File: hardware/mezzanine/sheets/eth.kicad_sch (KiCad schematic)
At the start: 6 parts, among them U3 TPD4EUSB30, U4 TPD4EUSB30, U5 MagJack-A70-112-331N126

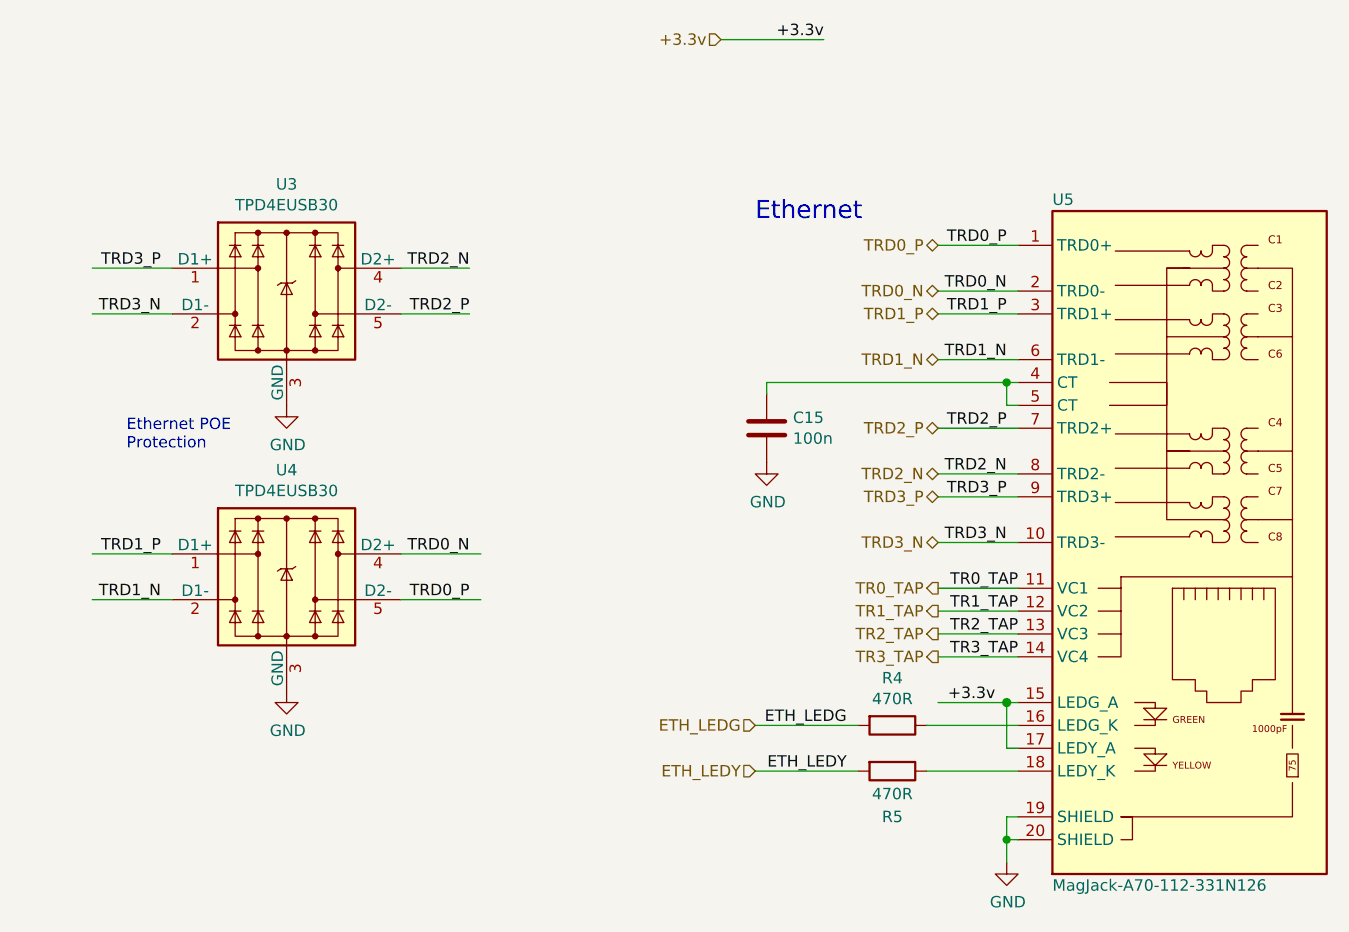
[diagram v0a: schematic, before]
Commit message: finished mezzanine signal routing
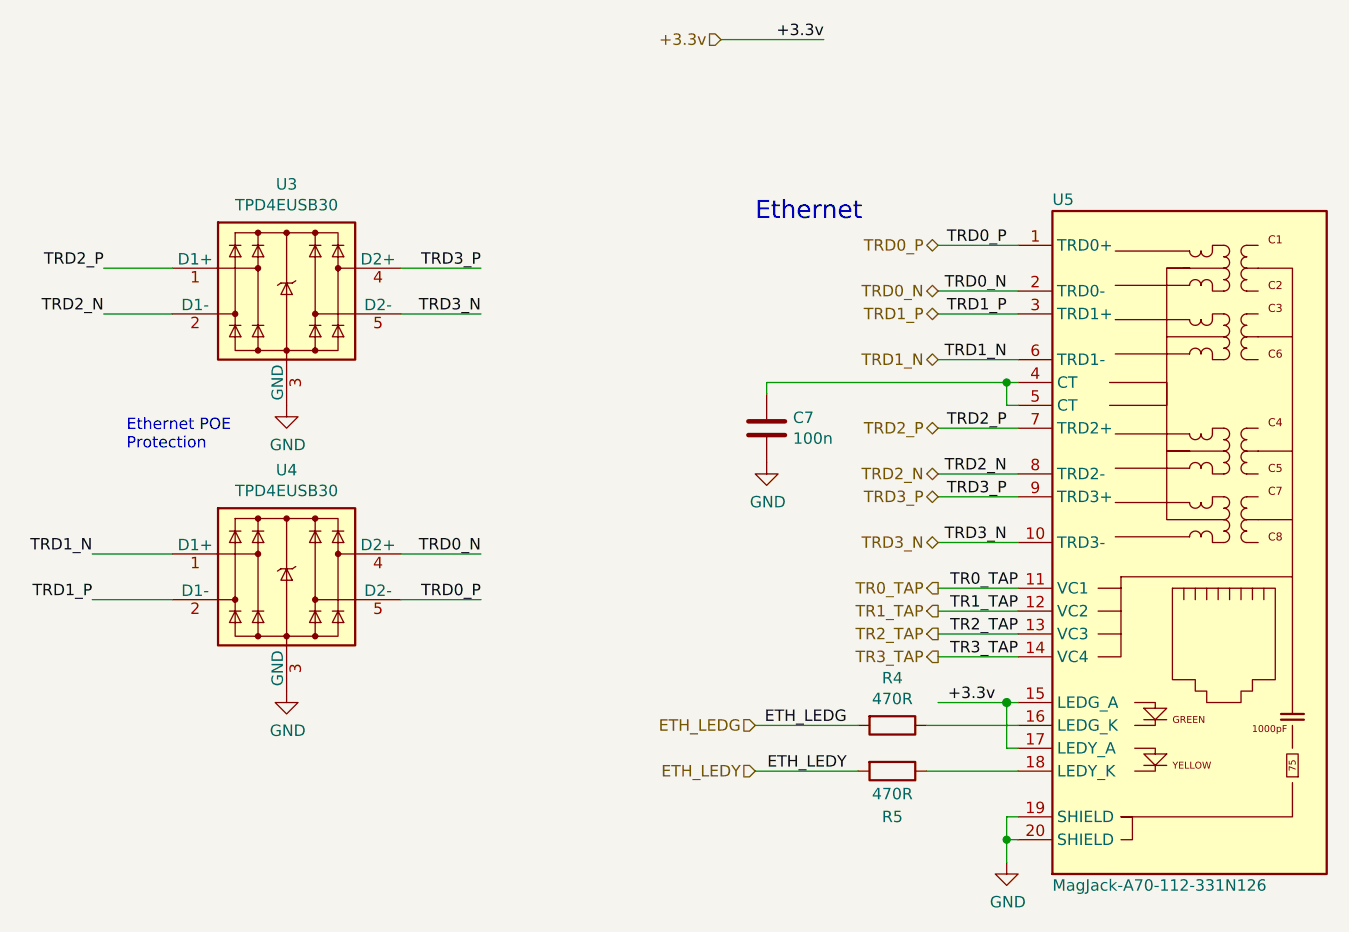
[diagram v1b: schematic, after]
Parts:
- C7: renamed from C15; footprint Capacitor_SMD:C_0402_1005Metric -> Capacitor_SMD:C_0603_1608Metric; Field4 Farnell -> (none); Field5 2611911 -> (none); Field6 RM EMK105 B7104KV-F -> (none); Field7 TAIYO YUDEN EUROPE GMBH -> (none); Field8 110091611 -> (none); Part Description 0.1uF 10% 16V Ceramic Capacitor X7R 0402 (1005 Metric) -> (none)
- R4, R5: footprint Resistor_SMD:R_0402_1005Metric -> Resistor_SMD:R_0603_1608Metric; Field4 Farnell -> (none); Field5 9239197 -> (none); Field6 RK73G1ETQTP4700D -> (none); Field7 KOA EUROPE GMBH -> (none); Field8 120887981 -> (none); Part Description Resistor 470R M1005 1% 63mW -> (none)
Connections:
- net TRD1_N: now also U4.1 (D1+), U4.10; no longer U4.2 (D1-), U4.9
- net TRD1_P: now also U4.2 (D1-), U4.9; no longer U4.1 (D1+), U4.10
- net TRD2_N: now also U3.2 (D1-), U3.9; no longer U3.4 (D2+), U3.7
- net TRD2_P: now also U3.1 (D1+), U3.10; no longer U3.5 (D2-), U3.6
- net TRD3_N: now also U3.5 (D2-), U3.6; no longer U3.2 (D1-), U3.9
- net TRD3_P: now also U3.4 (D2+), U3.7; no longer U3.1 (D1+), U3.10
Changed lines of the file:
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@@
   (junction (at 154.94 104.14) (diameter 1.016) (color 0 0 0 0))
   (junction (at 154.94 119.38) (diameter 0.9144) (color 0 0 0 0))
-  (wire (pts (xy 53.34 55.88) (xy 62.23 55.88))
-    (stroke (width 0) (type solid) (color 0 0 0 0))
-  )
-  (wire (pts (xy 53.34 60.96) (xy 62.23 60.96))
-    (stroke (width 0) (type solid) (color 0 0 0 0))
-  )
-  (wire (pts (xy 53.34 87.63) (xy 62.23 87.63))
-    (stroke (width 0) (type solid) (color 0 0 0 0))
-  )
-  (wire (pts (xy 62.23 92.71) (xy 53.34 92.71))
-    (stroke (width 0) (type solid) (color 0 0 0 0))
-  )
-  (wire (pts (xy 87.63 55.88) (xy 95.25 55.88))
-    (stroke (width 0) (type solid) (color 0 0 0 0))
-  )
-  (wire (pts (xy 87.63 60.96) (xy 95.25 60.96))
+  (wire (pts (xy 53.34 92.71) (xy 62.23 92.71))
+    (stroke (width 0) (type solid) (color 0 0 0 0))
+  )
+  (wire (pts (xy 54.61 55.88) (xy 62.23 55.88))
+    (stroke (width 0) (type solid) (color 0 0 0 0))
+  )
+  (wire (pts (xy 54.61 60.96) (xy 62.23 60.96))
+    (stroke (width 0) (type solid) (color 0 0 0 0))
+  )
+  (wire (pts (xy 62.23 87.63) (xy 53.34 87.63))
+    (stroke (width 0) (type solid) (color 0 0 0 0))
+  )
+  (wire (pts (xy 87.63 55.88) (xy 96.52 55.88))
+    (stroke (width 0) (type solid) (color 0 0 0 0))
+  )
+  (wire (pts (xy 87.63 60.96) (xy 96.52 60.96))
     (stroke (width 0) (type solid) (color 0 0 0 0))
   )
@@
     (effects (font (size 2.0066 2.0066)) (justify left bottom))
   )
-  (label "TRD3_P" (at 60.96 55.88 180)
-    (effects (font (size 1.27 1.27)) (justify right bottom))
-  )
-  (label "TRD3_N" (at 60.96 60.96 180)
-    (effects (font (size 1.27 1.27)) (justify right bottom))
-  )
-  (label "TRD1_P" (at 60.96 87.63 180)
-    (effects (font (size 1.27 1.27)) (justify right bottom))
-  )
-  (label "TRD1_N" (at 60.96 92.71 180)
-    (effects (font (size 1.27 1.27)) (justify right bottom))
-  )
-  (label "TRD2_N" (at 95.25 55.88 180)
-    (effects (font (size 1.27 1.27)) (justify right bottom))
-  )
-  (label "TRD2_P" (at 95.25 60.96 180)
-    (effects (font (size 1.27 1.27)) (justify right bottom))
-  )
-  (label "TRD0_N" (at 95.25 87.63 180)
-    (effects (font (size 1.27 1.27)) (justify right bottom))
-  )
-  (label "TRD0_P" (at 95.25 92.71 180)
+  (label "TRD1_N" (at 53.34 87.63 180)
+    (effects (font (size 1.27 1.27)) (justify right bottom))
+  )
+  (label "TRD1_P" (at 53.34 92.71 180)
+    (effects (font (size 1.27 1.27)) (justify right bottom))
+  )
+  (label "TRD2_P" (at 54.61 55.88 180)
+    (effects (font (size 1.27 1.27)) (justify right bottom))
+  )
+  (label "TRD2_N" (at 54.61 60.96 180)
+    (effects (font (size 1.27 1.27)) (justify right bottom))
+  )
+  (label "TRD3_P" (at 96.52 55.88 180)
+    (effects (font (size 1.27 1.27)) (justify right bottom))
+  )
+  (label "TRD3_N" (at 96.52 60.96 180)
+    (effects (font (size 1.27 1.27)) (justify right bottom))
+  )
+  (label "TRD0_N" (at 96.52 87.63 180)
+    (effects (font (size 1.27 1.27)) (justify right bottom))
+  )
+  (label "TRD0_P" (at 96.52 92.71 180)
     (effects (font (size 1.27 1.27)) (justify right bottom))
   )
@@
   (symbol (lib_id "power:GND") (at 74.93 71.12 0) (unit 1)
     (in_bom yes) (on_board yes)
-    (property "Reference" "#PWR068" (id 0) (at 74.93 77.47 0)
+    (property "Reference" "#PWR046" (id 0) (at 74.93 77.47 0)
       (effects (font (size 1.27 1.27)) hide)
     )
@@
   (symbol (lib_id "power:GND") (at 74.93 102.87 0) (unit 1)
     (in_bom yes) (on_board yes)
-    (property "Reference" "#PWR070" (id 0) (at 74.93 109.22 0)
+    (property "Reference" "#PWR048" (id 0) (at 74.93 109.22 0)
       (effects (font (size 1.27 1.27)) hide)
     )
@@
   (symbol (lib_id "power:GND") (at 128.27 77.47 0) (unit 1)
     (in_bom yes) (on_board yes)
-    (property "Reference" "#PWR069" (id 0) (at 128.27 83.82 0)
+    (property "Reference" "#PWR047" (id 0) (at 128.27 83.82 0)
       (effects (font (size 1.27 1.27)) hide)
     )
@@
   (symbol (lib_id "power:GND") (at 154.94 121.92 0) (unit 1)
     (in_bom yes) (on_board yes)
-    (property "Reference" "#PWR071" (id 0) (at 154.94 128.27 0)
+    (property "Reference" "#PWR049" (id 0) (at 154.94 128.27 0)
       (effects (font (size 1.27 1.27)) hide)
     )
@@
     (property "Reference" "R4" (id 0) (at 142.24 101.4222 90))
     (property "Value" "470R" (id 1) (at 142.24 103.7336 90))
-    (property "Footprint" "Resistor_SMD:R_0402_1005Metric" (id 2) (at 142.24 104.902 90)
-      (effects (font (size 1.27 1.27)) hide)
-    )
-    (property "Datasheet" "https://fscdn.rohm.com/en/products/databook/datasheet/passive/resistor/chip_resistor/mcr-e.pdf" (id 3) (at 142.24 106.68 0)
-      (effects (font (size 1.27 1.27)) hide)
-    )
-    (property "Field4" "Farnell" (id 4) (at 142.24 106.68 0)
-      (effects (font (size 1.27 1.27)) hide)
-    )
-    (property "Field5" "9239197" (id 5) (at 142.24 106.68 0)
-      (effects (font (size 1.27 1.27)) hide)
-    )
-    (property "Field7" "KOA EUROPE GMBH" (id 6) (at 142.24 106.68 0)
-      (effects (font (size 1.27 1.27)) hide)
-    )
-    (property "Field6" "RK73G1ETQTP4700D         " (id 7) (at 142.24 106.68 0)
-      (effects (font (size 1.27 1.27)) hide)
-    )
-    (property "Field8" "120887981" (id 8) (at 142.24 106.68 0)
-      (effects (font (size 1.27 1.27)) hide)
-    )
-    (property "Part Description" "Resistor 470R M1005 1% 63mW" (id 9) (at 142.24 106.68 0)
+    (property "Footprint" "Resistor_SMD:R_0603_1608Metric" (id 2) (at 142.24 104.902 90)
+      (effects (font (size 1.27 1.27)) hide)
+    )
+    (property "Datasheet" "~" (id 3) (at 142.24 106.68 0)
       (effects (font (size 1.27 1.27)) hide)
     )
@@
     (property "Reference" "R5" (id 0) (at 142.24 116.84 90))
     (property "Value" "470R" (id 1) (at 142.24 114.3 90))
-    (property "Footprint" "Resistor_SMD:R_0402_1005Metric" (id 2) (at 142.24 109.982 90)
-      (effects (font (size 1.27 1.27)) hide)
-    )
-    (property "Datasheet" "https://fscdn.rohm.com/en/products/databook/datasheet/passive/resistor/chip_resistor/mcr-e.pdf" (id 3) (at 142.24 111.76 0)
-      (effects (font (size 1.27 1.27)) hide)
-    )
-    (property "Field4" "Farnell" (id 4) (at 142.24 111.76 0)
-      (effects (font (size 1.27 1.27)) hide)
-    )
-    (property "Field5" "9239197" (id 5) (at 142.24 111.76 0)
-      (effects (font (size 1.27 1.27)) hide)
-    )
-    (property "Field7" "KOA EUROPE GMBH" (id 6) (at 142.24 111.76 0)
-      (effects (font (size 1.27 1.27)) hide)
-    )
-    (property "Field6" "RK73G1ETQTP4700D         " (id 7) (at 142.24 111.76 0)
-      (effects (font (size 1.27 1.27)) hide)
-    )
-    (property "Field8" "120887981" (id 8) (at 142.24 111.76 0)
-      (effects (font (size 1.27 1.27)) hide)
-    )
-    (property "Part Description" "Resistor 470R M1005 1% 63mW" (id 9) (at 142.24 111.76 0)
+    (property "Footprint" "Resistor_SMD:R_0603_1608Metric" (id 2) (at 142.24 109.982 90)
+      (effects (font (size 1.27 1.27)) hide)
+    )
+    (property "Datasheet" "~" (id 3) (at 142.24 111.76 0)
       (effects (font (size 1.27 1.27)) hide)
     )
@@
   (symbol (lib_id "Device:C") (at 128.27 73.66 0) (unit 1)
     (in_bom yes) (on_board yes)
-    (property "Reference" "C15" (id 0) (at 131.191 72.4916 0)
+    (property "Reference" "C7" (id 0) (at 131.191 72.4916 0)
       (effects (font (size 1.27 1.27)) (justify left))
     )
@@
       (effects (font (size 1.27 1.27)) (justify left))
     )
-    (property "Footprint" "Capacitor_SMD:C_0402_1005Metric" (id 2) (at 129.2352 77.47 0)
-      (effects (font (size 1.27 1.27)) hide)
-    )
-    (property "Datasheet" "https://search.murata.co.jp/Ceramy/image/img/A01X/G101/ENG/GRM155R71C104KA88-01.pdf" (id 3) (at 128.27 73.66 0)
-      (effects (font (size 1.27 1.27)) hide)
-    )
-    (property "Field4" "Farnell" (id 4) (at 128.27 73.66 0)
-      (effects (font (size 1.27 1.27)) hide)
-    )
-    (property "Field5" "2611911" (id 5) (at 128.27 73.66 0)
-      (effects (font (size 1.27 1.27)) hide)
-    )
-    (property "Field6" "RM EMK105 B7104KV-F" (id 6) (at 128.27 73.66 0)
-      (effects (font (size 1.27 1.27)) hide)
-    )
-    (property "Field7" "TAIYO YUDEN EUROPE GMBH" (id 7) (at 128.27 73.66 0)
-      (effects (font (size 1.27 1.27)) hide)
-    )
-    (property "Part Description" "	0.1uF 10% 16V Ceramic Capacitor X7R 0402 (1005 Metric)" (id 8) (at 128.27 73.66 0)
-      (effects (font (size 1.27 1.27)) hide)
-    )
-    (property "Field8" "110091611" (id 9) (at 128.27 73.66 0)
-      (effects (font (size 1.27 1.27)) hide)
-    )
+    (property "Footprint" "Capacitor_SMD:C_0603_1608Metric" (id 2) (at 129.2352 77.47 0)
+      (effects (font (size 1.27 1.27)) hide)
+    )
+    (property "Datasheet" "~" (id 3) (at 128.27 73.66 0)
+      (effects (font (size 1.27 1.27)) hide)
+    )

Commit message: sheet refs relative, copied escalator pinout to lobby
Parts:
- renumbered C7 to C?, R5 to R?, R4 to R?, U5 to U?, U4 to U?, U3 to U?
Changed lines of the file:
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@@
   (symbol (lib_id "power:GND") (at 74.93 71.12 0) (unit 1)
     (in_bom yes) (on_board yes)
-    (property "Reference" "#PWR046" (id 0) (at 74.93 77.47 0)
+    (property "Reference" "#PWR?" (id 0) (at 74.93 77.47 0)
       (effects (font (size 1.27 1.27)) hide)
     )
@@
   (symbol (lib_id "power:GND") (at 74.93 102.87 0) (unit 1)
     (in_bom yes) (on_board yes)
-    (property "Reference" "#PWR048" (id 0) (at 74.93 109.22 0)
+    (property "Reference" "#PWR?" (id 0) (at 74.93 109.22 0)
       (effects (font (size 1.27 1.27)) hide)
     )
@@
   (symbol (lib_id "power:GND") (at 128.27 77.47 0) (unit 1)
     (in_bom yes) (on_board yes)
-    (property "Reference" "#PWR047" (id 0) (at 128.27 83.82 0)
+    (property "Reference" "#PWR?" (id 0) (at 128.27 83.82 0)
       (effects (font (size 1.27 1.27)) hide)
     )
@@
   (symbol (lib_id "power:GND") (at 154.94 121.92 0) (unit 1)
     (in_bom yes) (on_board yes)
-    (property "Reference" "#PWR049" (id 0) (at 154.94 128.27 0)
+    (property "Reference" "#PWR?" (id 0) (at 154.94 128.27 0)
       (effects (font (size 1.27 1.27)) hide)
     )
@@
   (symbol (lib_id "Device:R") (at 142.24 106.68 270) (unit 1)
     (in_bom yes) (on_board yes)
-    (property "Reference" "R4" (id 0) (at 142.24 101.4222 90))
+    (property "Reference" "R?" (id 0) (at 142.24 101.4222 90))
     (property "Value" "470R" (id 1) (at 142.24 103.7336 90))
     (property "Footprint" "Resistor_SMD:R_0603_1608Metric" (id 2) (at 142.24 104.902 90)
@@
   (symbol (lib_id "Device:R") (at 142.24 111.76 270) (unit 1)
     (in_bom yes) (on_board yes)
-    (property "Reference" "R5" (id 0) (at 142.24 116.84 90))
+    (property "Reference" "R?" (id 0) (at 142.24 116.84 90))
     (property "Value" "470R" (id 1) (at 142.24 114.3 90))
     (property "Footprint" "Resistor_SMD:R_0603_1608Metric" (id 2) (at 142.24 109.982 90)
@@
   (symbol (lib_id "Device:C") (at 128.27 73.66 0) (unit 1)
     (in_bom yes) (on_board yes)
-    (property "Reference" "C7" (id 0) (at 131.191 72.4916 0)
+    (property "Reference" "C?" (id 0) (at 131.191 72.4916 0)
       (effects (font (size 1.27 1.27)) (justify left))
     )
@@
   (symbol (lib_id "CM4IO:TPD4EUSB30") (at 74.93 58.42 0) (unit 1)
     (in_bom yes) (on_board yes)
-    (property "Reference" "U3" (id 0) (at 74.93 46.5582 0))
+    (property "Reference" "U?" (id 0) (at 74.93 46.5582 0))
     (property "Value" "TPD4EUSB30" (id 1) (at 74.93 48.8696 0))
     (property "Footprint" "Package_SON:USON-10_2.5x1.0mm_P0.5mm" (id 2) (at 50.8 68.58 0)
@@
   (symbol (lib_id "CM4IO:TPD4EUSB30") (at 74.93 90.17 0) (unit 1)
     (in_bom yes) (on_board yes)
-    (property "Reference" "U4" (id 0) (at 74.93 78.3082 0))
+    (property "Reference" "U?" (id 0) (at 74.93 78.3082 0))
     (property "Value" "TPD4EUSB30" (id 1) (at 74.93 80.6196 0))
     (property "Footprint" "Package_SON:USON-10_2.5x1.0mm_P0.5mm" (id 2) (at 50.8 100.33 0)
@@
   (symbol (lib_id "CM4IO:MagJack-A70-112-331N126") (at 177.8 124.46 0) (unit 1)
     (in_bom yes) (on_board yes)
-    (property "Reference" "U5" (id 0) (at 160.02 48.26 0)
+    (property "Reference" "U?" (id 0) (at 160.02 48.26 0)
       (effects (font (size 1.27 1.27)) (justify left))
     )

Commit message: addtl hdmi routing
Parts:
- gave numbers to parts that had none: 6
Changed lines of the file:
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@@
   (symbol (lib_id "power:GND") (at 74.93 71.12 0) (unit 1)
     (in_bom yes) (on_board yes)
-    (property "Reference" "#PWR?" (id 0) (at 74.93 77.47 0)
+    (property "Reference" "#PWR0119" (id 0) (at 74.93 77.47 0)
       (effects (font (size 1.27 1.27)) hide)
     )
@@
   (symbol (lib_id "power:GND") (at 74.93 102.87 0) (unit 1)
     (in_bom yes) (on_board yes)
-    (property "Reference" "#PWR?" (id 0) (at 74.93 109.22 0)
+    (property "Reference" "#PWR0117" (id 0) (at 74.93 109.22 0)
       (effects (font (size 1.27 1.27)) hide)
     )
@@
   (symbol (lib_id "power:GND") (at 128.27 77.47 0) (unit 1)
     (in_bom yes) (on_board yes)
-    (property "Reference" "#PWR?" (id 0) (at 128.27 83.82 0)
+    (property "Reference" "#PWR0118" (id 0) (at 128.27 83.82 0)
       (effects (font (size 1.27 1.27)) hide)
     )
@@
   (symbol (lib_id "power:GND") (at 154.94 121.92 0) (unit 1)
     (in_bom yes) (on_board yes)
-    (property "Reference" "#PWR?" (id 0) (at 154.94 128.27 0)
+    (property "Reference" "#PWR0116" (id 0) (at 154.94 128.27 0)
       (effects (font (size 1.27 1.27)) hide)
     )
@@
   (symbol (lib_id "Device:R") (at 142.24 106.68 270) (unit 1)
     (in_bom yes) (on_board yes)
-    (property "Reference" "R?" (id 0) (at 142.24 101.4222 90))
+    (property "Reference" "R4" (id 0) (at 142.24 101.4222 90))
     (property "Value" "470R" (id 1) (at 142.24 103.7336 90))
     (property "Footprint" "Resistor_SMD:R_0603_1608Metric" (id 2) (at 142.24 104.902 90)
@@
   (symbol (lib_id "Device:R") (at 142.24 111.76 270) (unit 1)
     (in_bom yes) (on_board yes)
-    (property "Reference" "R?" (id 0) (at 142.24 116.84 90))
+    (property "Reference" "R5" (id 0) (at 142.24 116.84 90))
     (property "Value" "470R" (id 1) (at 142.24 114.3 90))
     (property "Footprint" "Resistor_SMD:R_0603_1608Metric" (id 2) (at 142.24 109.982 90)
@@
   (symbol (lib_id "Device:C") (at 128.27 73.66 0) (unit 1)
     (in_bom yes) (on_board yes)
-    (property "Reference" "C?" (id 0) (at 131.191 72.4916 0)
+    (property "Reference" "C7" (id 0) (at 131.191 72.4916 0)
       (effects (font (size 1.27 1.27)) (justify left))
     )
@@
   (symbol (lib_id "CM4IO:TPD4EUSB30") (at 74.93 58.42 0) (unit 1)
     (in_bom yes) (on_board yes)
-    (property "Reference" "U?" (id 0) (at 74.93 46.5582 0))
+    (property "Reference" "U3" (id 0) (at 74.93 46.5582 0))
     (property "Value" "TPD4EUSB30" (id 1) (at 74.93 48.8696 0))
     (property "Footprint" "Package_SON:USON-10_2.5x1.0mm_P0.5mm" (id 2) (at 50.8 68.58 0)
@@
   (symbol (lib_id "CM4IO:TPD4EUSB30") (at 74.93 90.17 0) (unit 1)
     (in_bom yes) (on_board yes)
-    (property "Reference" "U?" (id 0) (at 74.93 78.3082 0))
+    (property "Reference" "U4" (id 0) (at 74.93 78.3082 0))
     (property "Value" "TPD4EUSB30" (id 1) (at 74.93 80.6196 0))
     (property "Footprint" "Package_SON:USON-10_2.5x1.0mm_P0.5mm" (id 2) (at 50.8 100.33 0)
@@
   (symbol (lib_id "CM4IO:MagJack-A70-112-331N126") (at 177.8 124.46 0) (unit 1)
     (in_bom yes) (on_board yes)
-    (property "Reference" "U?" (id 0) (at 160.02 48.26 0)
+    (property "Reference" "U5" (id 0) (at 160.02 48.26 0)
       (effects (font (size 1.27 1.27)) (justify left))
     )
